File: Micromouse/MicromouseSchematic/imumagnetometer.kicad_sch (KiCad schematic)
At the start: 14 parts, among them J11 Conn_01x07_Pin, U3 ICM-42688-P, U4 LIS2MDLTR

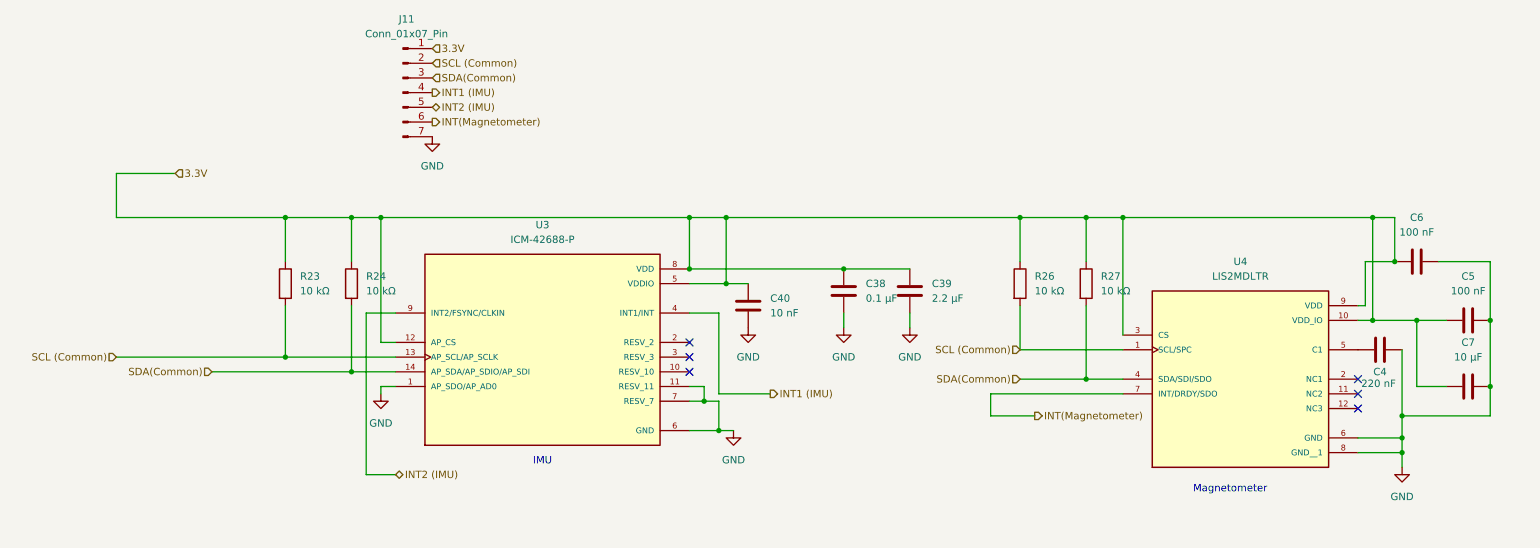
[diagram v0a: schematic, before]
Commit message: Fixed motor driver
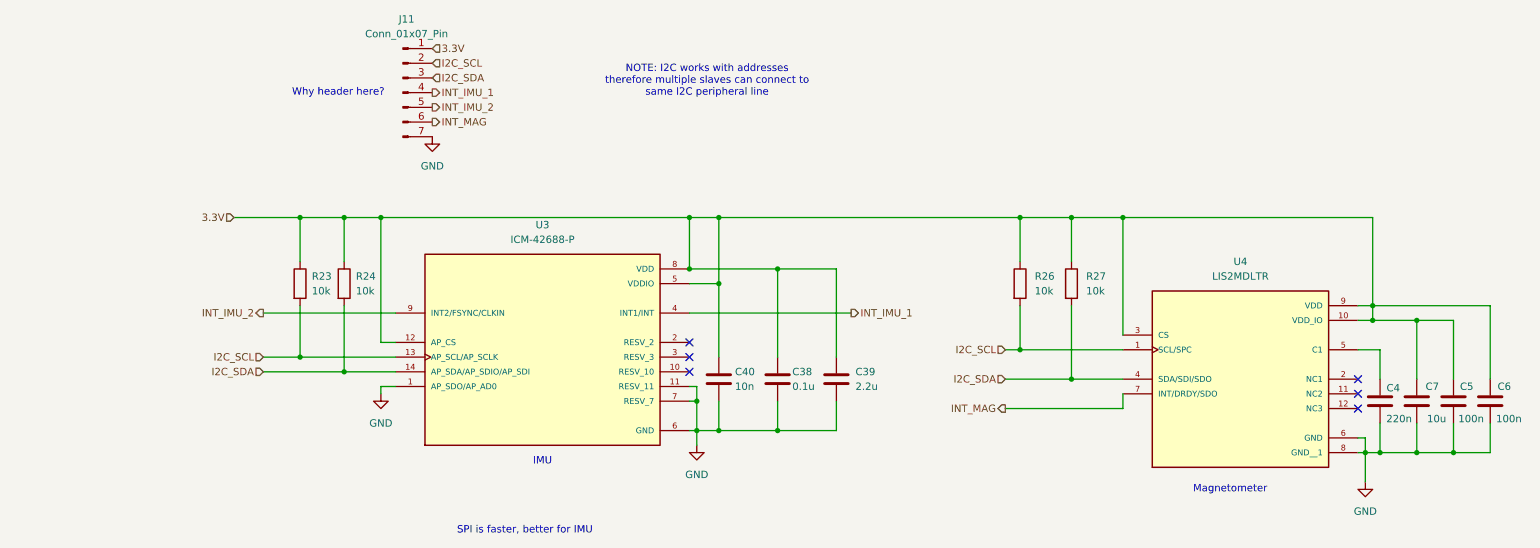
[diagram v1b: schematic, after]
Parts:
- C38: value 0.1 μF -> 0.1u
- C39: value 2.2 μF -> 2.2u
- C4: value 220 nF -> 220n
- C40: value 10 nF -> 10n
- C5, C6: value 100 nF -> 100n
- C7: value 10 μF -> 10u
- R23, R24, R26, R27: value 10 kΩ -> 10k
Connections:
- net 3.3V: now also C5.2, C7.2; no longer C5.1, C7.1
- net GND: now also C4.1, C5.1, C7.1; no longer C4.2, C5.2, C7.2
- net at U4.5 (C1): now also C4.2; no longer C4.1
- net INT(Magnetometer) renamed INT_MAG
- net INT1 (IMU) renamed INT_IMU_1
- net INT2 (IMU) renamed INT_IMU_2
- net SCL (Common) renamed I2C_SCL
- net SDA(Common) renamed I2C_SDA
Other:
- note added: "NOTE: I2C works with addresses therefore multiple slaves can connect to same I2C peripheral line"
- note added: "SPI is faster, better for IMU"
- note added: "Why header here?"
- moved on the sheet: C38, C39, C4, C40, C5, C6, C7, R23, R24, R27
